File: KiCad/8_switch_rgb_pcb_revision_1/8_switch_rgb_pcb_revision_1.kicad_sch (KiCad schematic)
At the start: 95 parts, among them SW0 SW0, SW1 SW1, SW2 SW2, SW3 SW3, SW4 SW4, SW5 SW5, SW6 SW6, SW7 SW7, U2 74HC165, Y1 16MHz

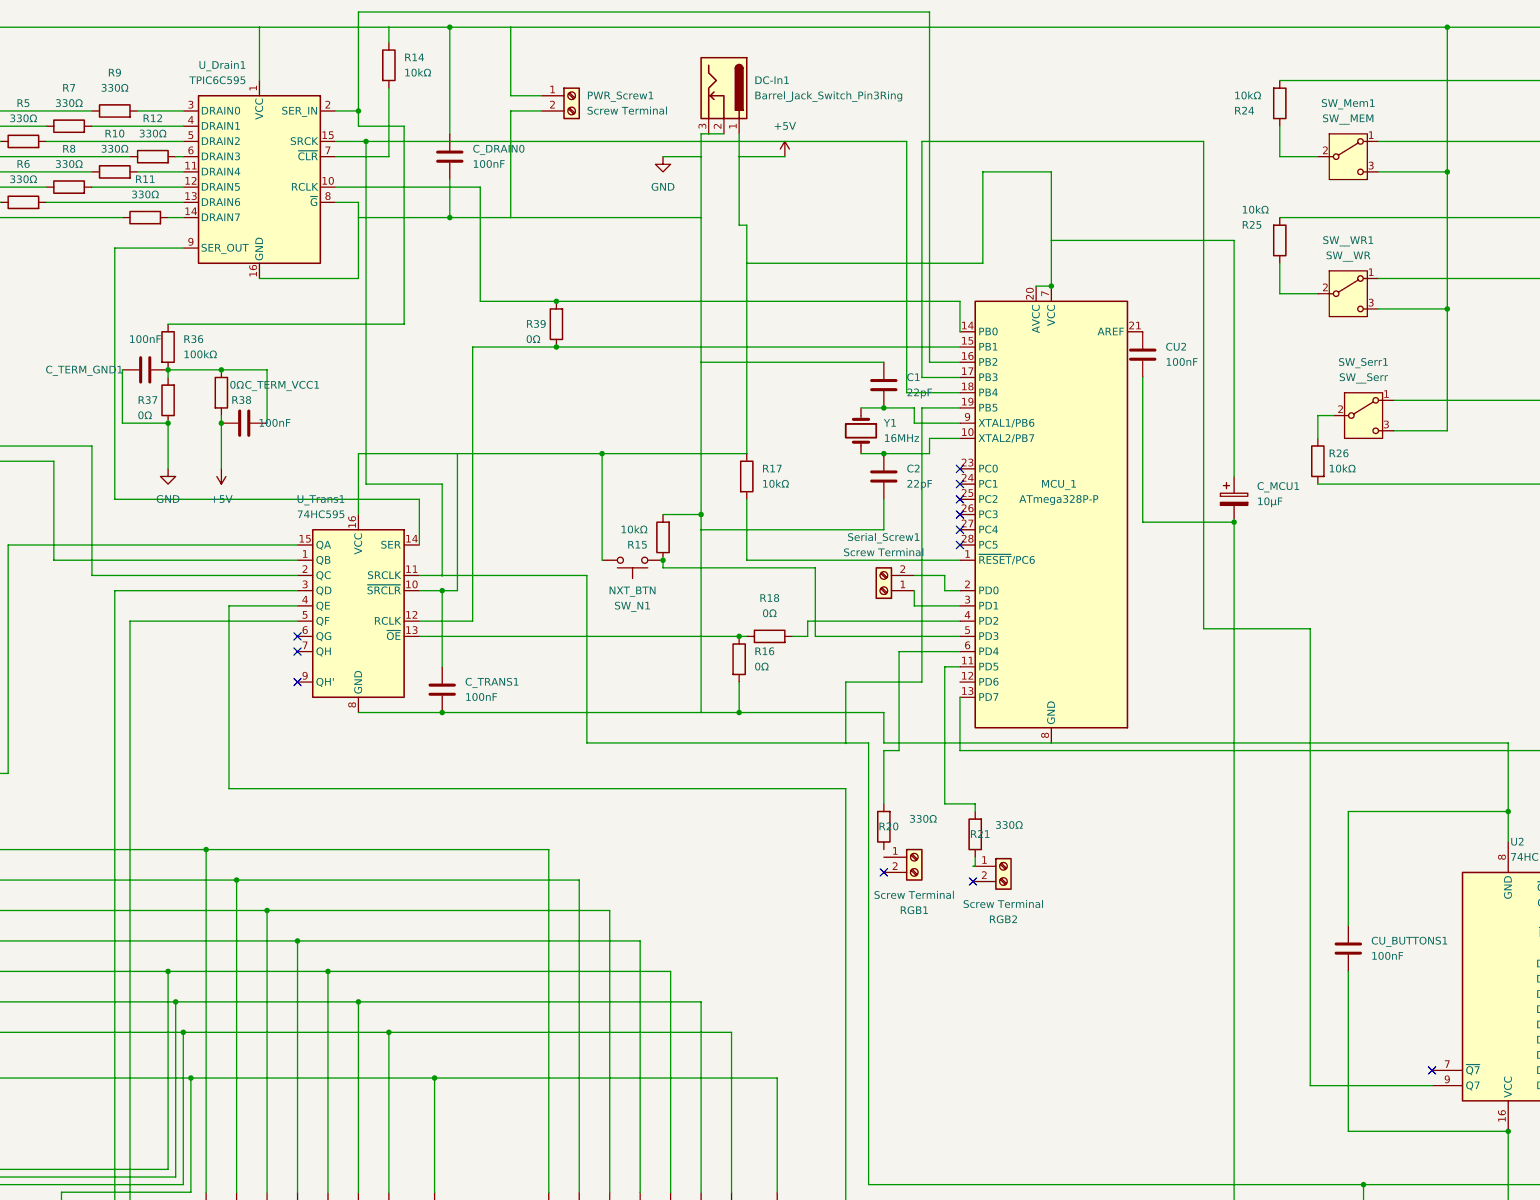
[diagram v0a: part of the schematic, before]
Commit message: Added 33 ohm series termination resistors. In series with all clock and dataoutputs
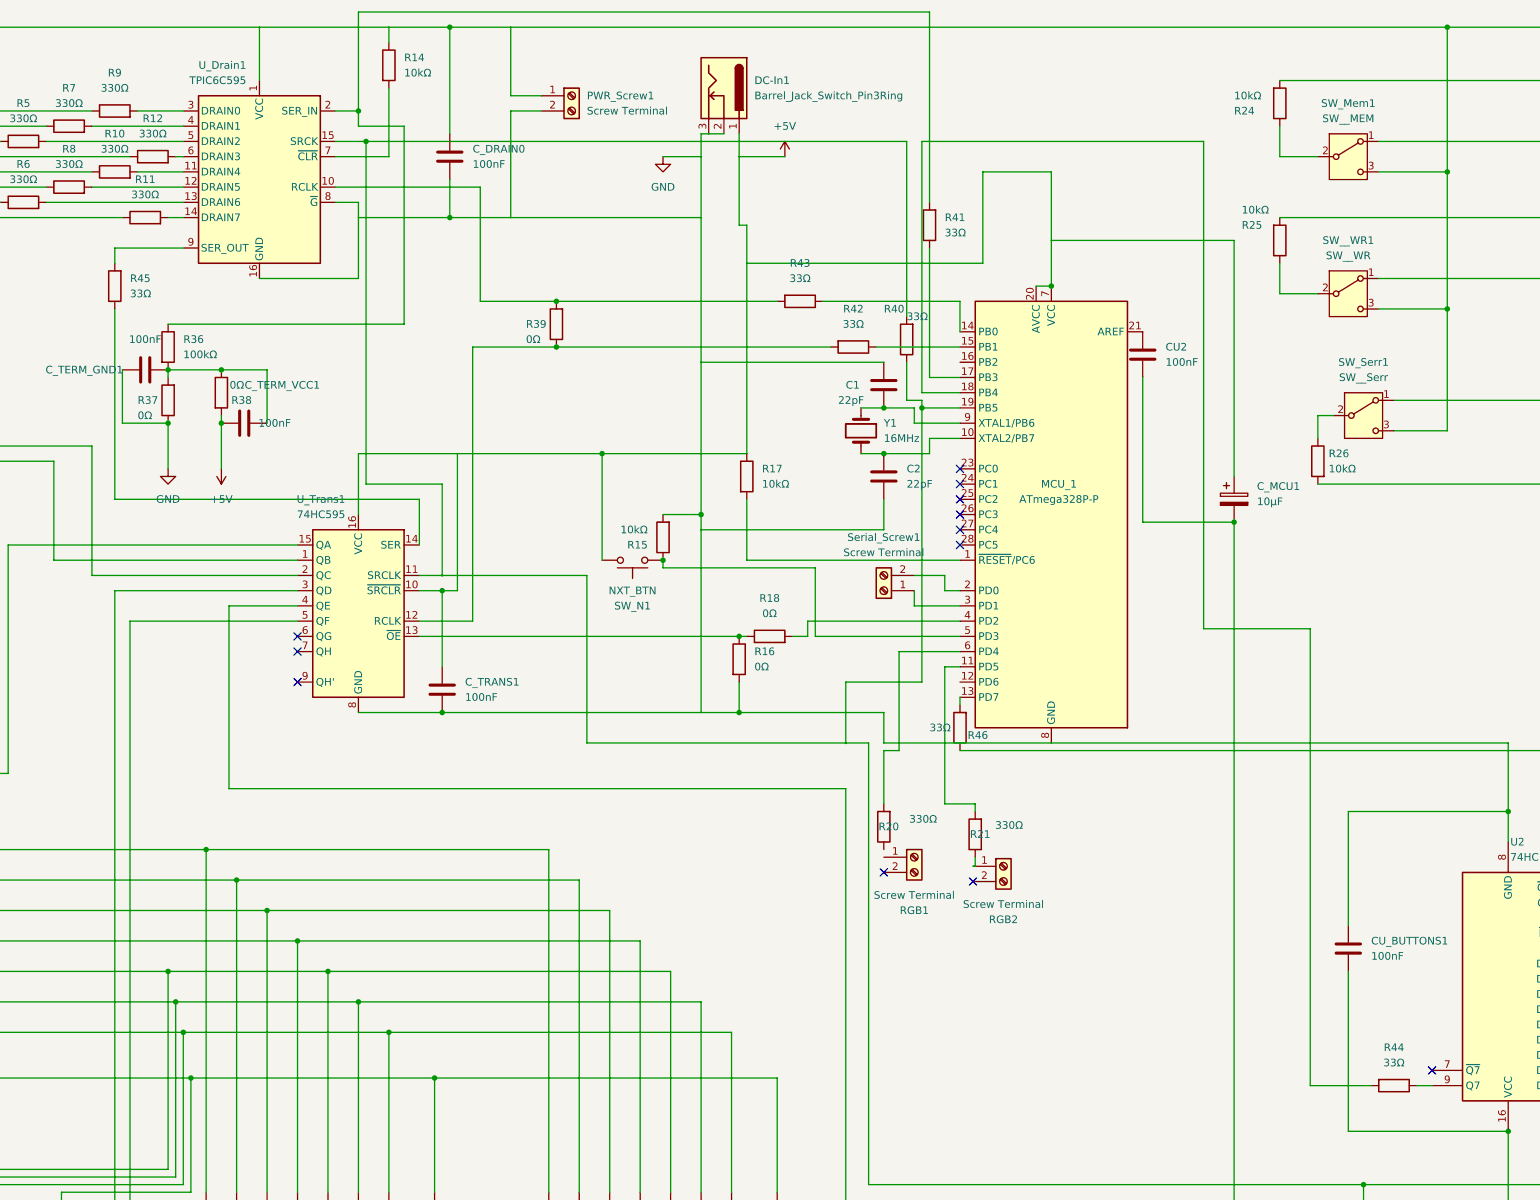
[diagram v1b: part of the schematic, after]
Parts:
- added R40, R41, R42, R43, R44, R45, R46: 33Ω, Resistor_THT:R_Axial_DIN0204_L3.6mm_D1.6mm_P5.08mm_Horizontal, symbol Device:R
- R39: footprint Resistor_THT:R_Axial_DIN0204_L3.6mm_D1.6mm_P2.54mm_Vertical -> Resistor_THT:R_Axial_DIN0204_L3.6mm_D1.6mm_P5.08mm_Horizontal
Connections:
- net at R36.1, U_Drain1.2 (SER_IN): now also R41.2; no longer MCU_1.16 (PB2)
- net at U2.1 (~{PL}): now also R46.1; no longer MCU_1.13 (PD7)
- net at MCU_1.19 (PB5), R22.1, U2.2 (CP)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: now also R40.1, R40.2; no longer MCU_1.18 (PB4)
- net at U2.9 (Q7): now also R44.1; no longer MCU_1.17 (PB3)
- net at R39.1, U_Trans1.12 (RCLK): now also R42.2; no longer MCU_1.15 (PB1)
- net at U_Trans1.14 (SER): now also R45.1; no longer U_Drain1.9 (SER_OUT)
- net at R39.2, U_Drain1.10 (RCLK): now also R43.2; no longer MCU_1.14 (PB0)
- new net: MCU_1.13 (PD7), R46.2
- new net: R45.2, U_Drain1.9 (SER_OUT)
- new net: MCU_1.15 (PB1), R42.1
- new net: MCU_1.14 (PB0), R43.1
- new net: MCU_1.17 (PB3), R41.1
- new net: MCU_1.18 (PB4), R44.2

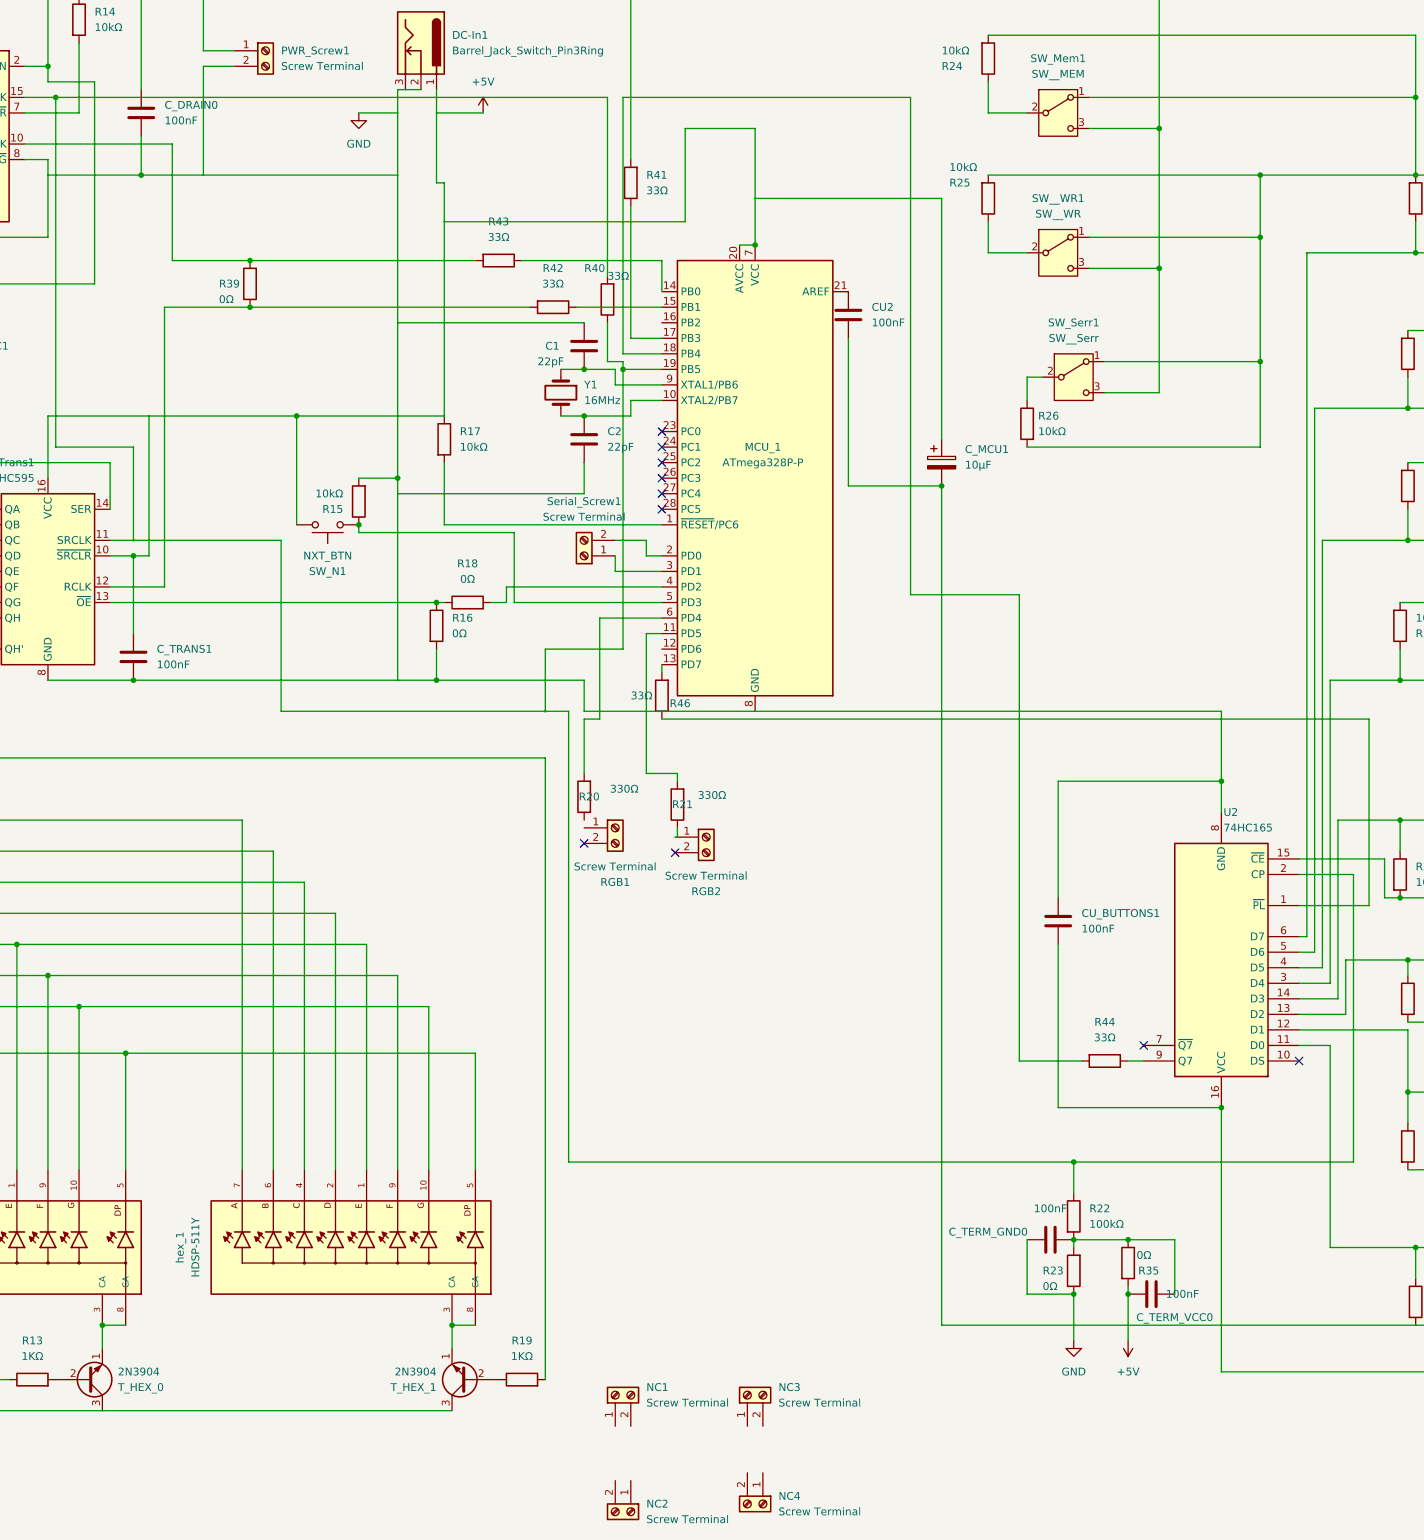
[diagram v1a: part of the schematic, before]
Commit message: Added all components to board. But the amount of terrible track management is impossible without sleep. I had hopped to be done today, but the remaining tracks and DRC-check will take 2 hours, 4-8 if i'm tired and keep shooting my own foot.
The important data and clock need to be keept in acute memory.
Data and clock includes OE and register-clocks.

I tracked them at the verry begining, so it should be fine.
Just need to be REALLY careful.
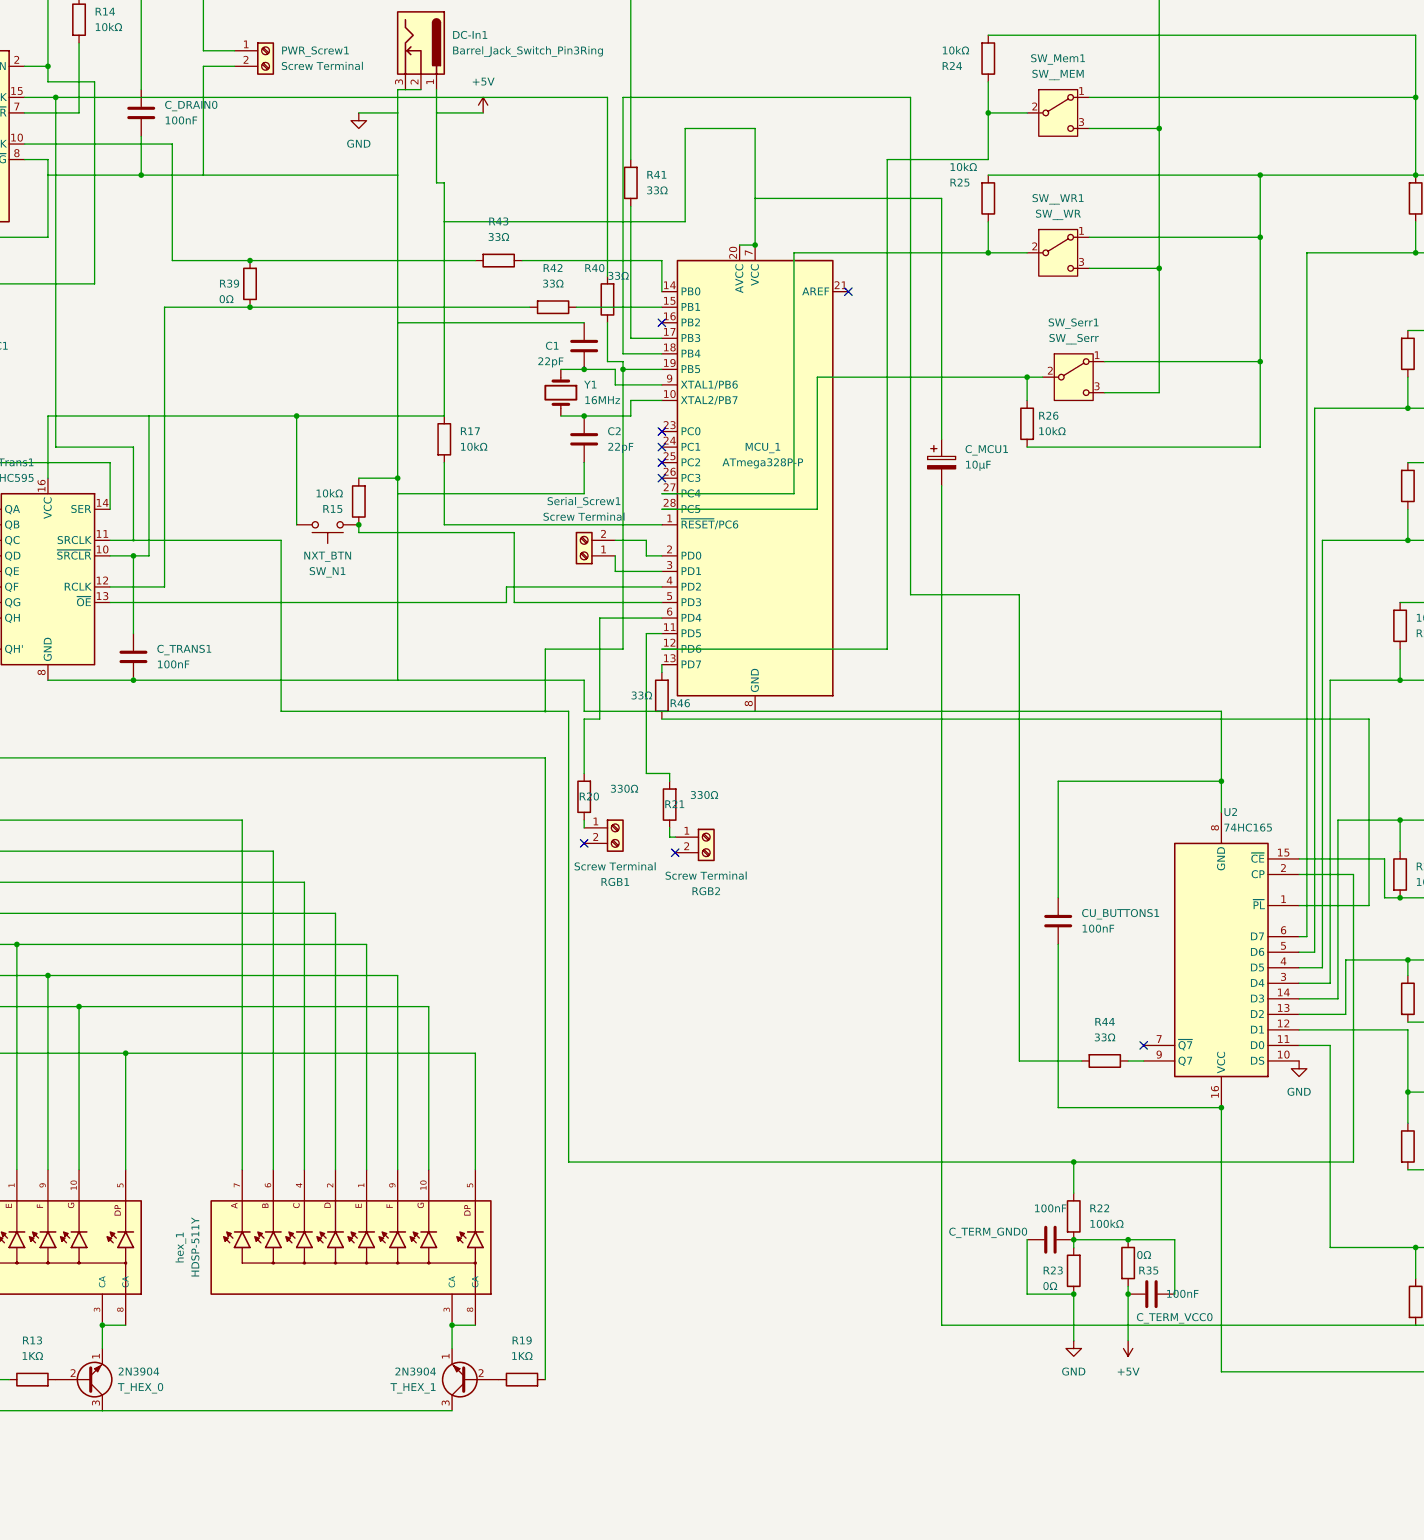
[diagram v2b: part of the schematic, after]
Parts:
- removed CU2: 100nF, Capacitor_THT:C_Disc_D5.0mm_W2.5mm_P5.00mm, symbol Device:C
- removed NC1, NC2, NC3, NC4: Screw Terminal, TerminalBlock_Phoenix:TerminalBlock_Phoenix_MPT-0,5-2-2.54_1x02_P2.54mm_Horizontal, symbol Connector:Screw_Terminal_01x02
- removed R16, R18: 0Ω, Resistor_THT:R_Axial_DIN0204_L3.6mm_D1.6mm_P2.54mm_Vertical, symbol Device:R
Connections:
- net GND: now also U2.10 (DS)
- net at R24.1, SW_Mem1.2 (B): now also MCU_1.12 (PD6)
- net at U_Trans1.13 (~{OE}): now also MCU_1.4 (PD2)
- net at R20.1: now also RGB1.1 (Pin_1)
- net at MCU_1.27 (PC4): now also R25.1, SW__WR1.2 (B)
- net at MCU_1.28 (PC5): now also R26.1, SW_Serr1.2 (B)
- no-connect marks 13 -> 12
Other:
- moved on the sheet: R21
